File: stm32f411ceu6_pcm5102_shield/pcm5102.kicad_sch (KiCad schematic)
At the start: 29 parts, among them J200 AudioJack3_Ground_SwitchTR, J201 Conn_01x03_Pin, SW200 SW_DPDT_XLX, U200 PCM5102A, U201 HT7533-1

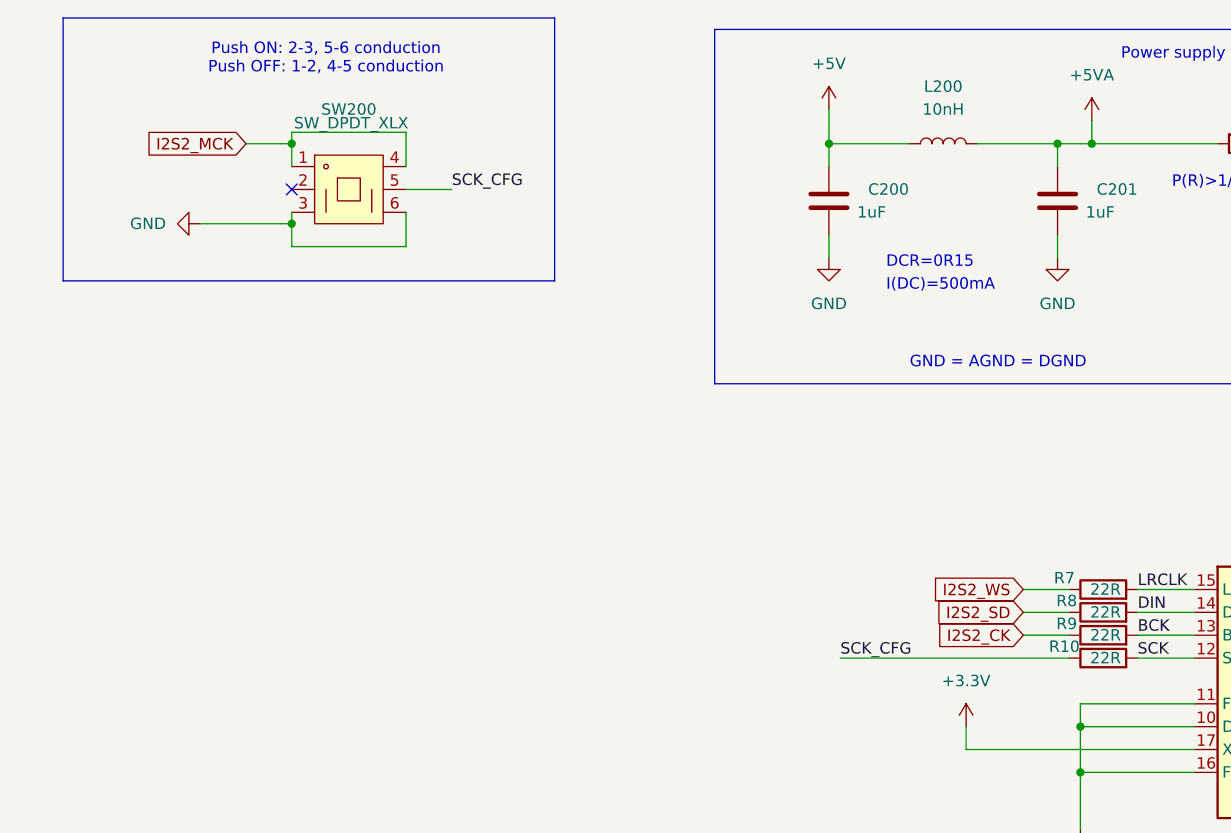
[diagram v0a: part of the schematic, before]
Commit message: First PCB routing
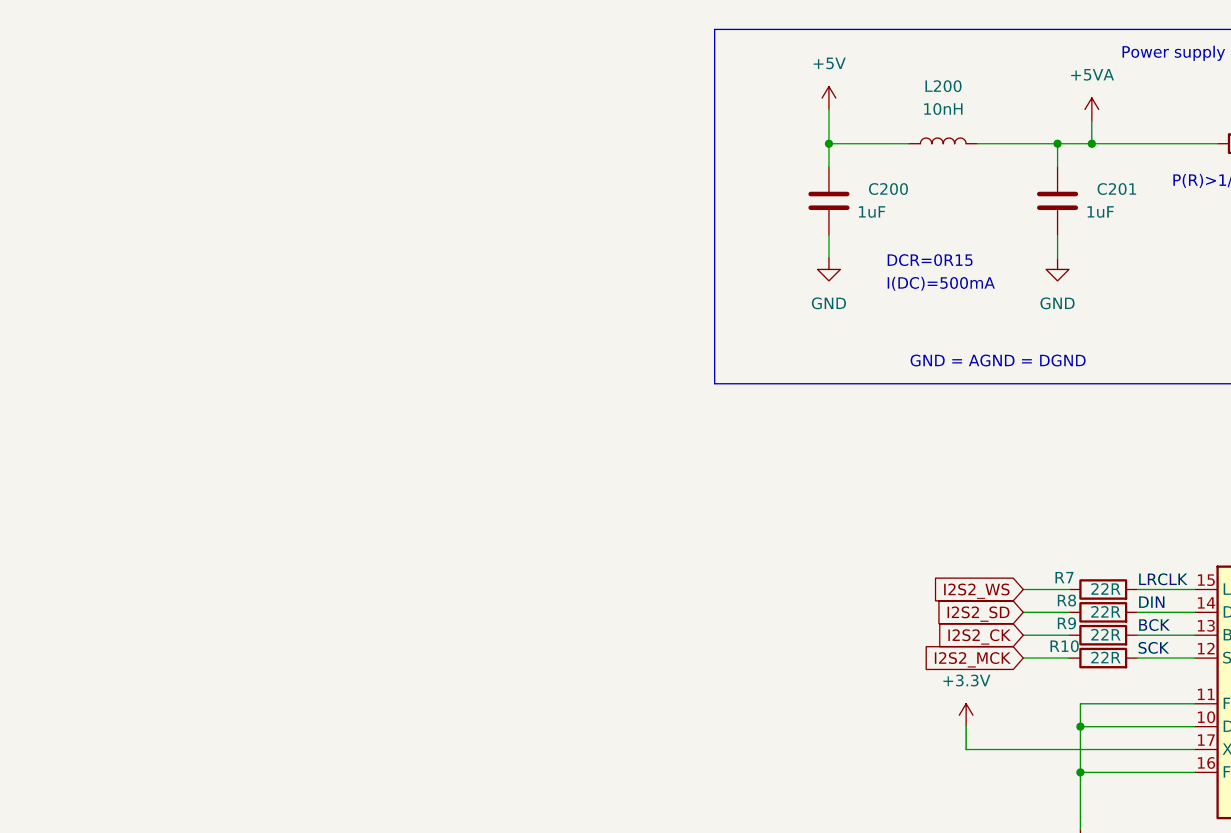
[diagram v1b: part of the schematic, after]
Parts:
- removed SW200: SW_DPDT_XLX, stm32f401_pcm5102_shiled_lib:SW_DPDT_XLX, symbol stm32f401_pcm5102_shiled_lib:SW_DPDT_XLX
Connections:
- net SCK_CFG is gone; now on net I2S2_MCK: R10.1
- no-connect marks 1 -> 0
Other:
- note removed: "Push ON: 2-3, 5-6 conduction Push OFF: 1-2, 4-5 conduction"

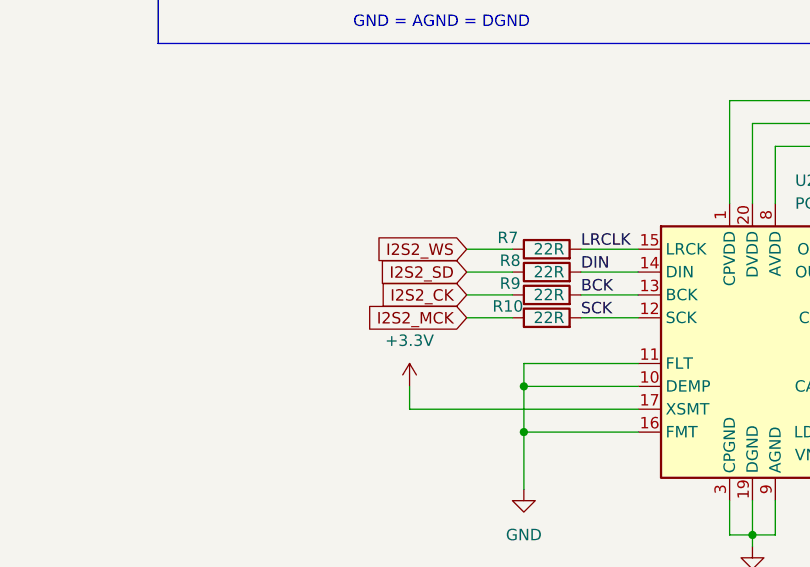
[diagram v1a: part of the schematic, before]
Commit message: Update firmware to simplify routing
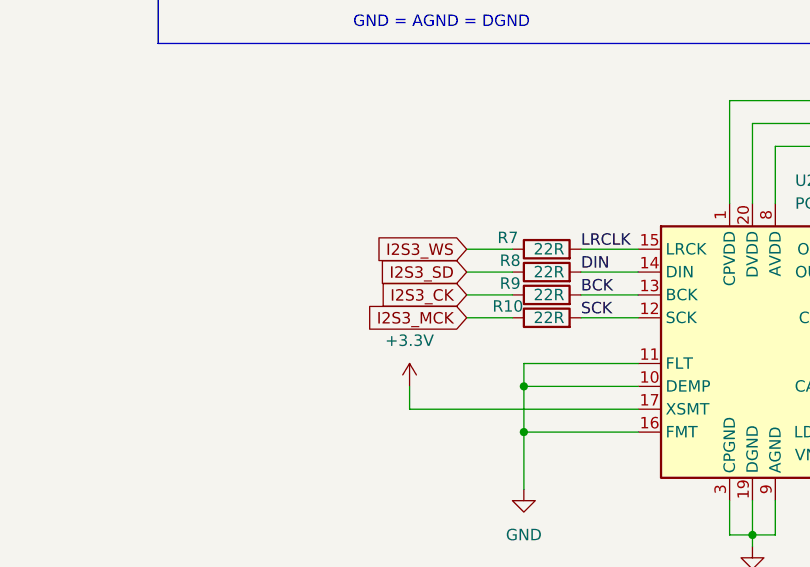
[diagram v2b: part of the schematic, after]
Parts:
- R10, R7, R8, R9: footprint Resistor_SMD:R_0805_2012Metric -> Resistor_SMD:R_0603_1608Metric
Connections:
- net I2S2_CK renamed I2S3_CK
- net I2S2_MCK renamed I2S3_MCK
- net I2S2_SD renamed I2S3_SD
- net I2S2_WS renamed I2S3_WS
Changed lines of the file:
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@@
 		)
 	)
-	(global_label "I2S2_CK"
+	(global_label "I2S3_CK"
 		(shape input)
 		(at 120.65 81.28 180)
@@
 		)
 	)
-	(global_label "I2S2_SD"
+	(global_label "I2S3_SD"
 		(shape input)
 		(at 120.65 78.74 180)
@@
 		)
 	)
-	(global_label "I2S2_WS"
+	(global_label "I2S3_WS"
 		(shape input)
 		(at 120.65 76.2 180)
@@
 		)
 	)
-	(global_label "I2S2_MCK"
+	(global_label "I2S3_MCK"
 		(shape input)
 		(at 120.65 83.82 180)
@@
 			)
 		)
-		(property "Footprint" "Resistor_SMD:R_0805_2012Metric"
+		(property "Footprint" "Resistor_SMD:R_0603_1608Metric"
 			(at 129.54 83.058 90)
 			(effects
@@
 			)
 		)
-		(property "Footprint" "Resistor_SMD:R_0805_2012Metric"
+		(property "Footprint" "Resistor_SMD:R_0603_1608Metric"
 			(at 129.54 85.598 90)
 			(effects
@@
 			)
 		)
-		(property "Footprint" "Resistor_SMD:R_0805_2012Metric"
+		(property "Footprint" "Resistor_SMD:R_0603_1608Metric"
 			(at 129.54 77.978 90)
 			(effects
@@
 			)
 		)
-		(property "Footprint" "Resistor_SMD:R_0805_2012Metric"
+		(property "Footprint" "Resistor_SMD:R_0603_1608Metric"
 			(at 129.54 80.518 90)
 			(effects

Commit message: BOM fixes
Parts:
- R10, R7, R8, R9: Manufacturer Part Number 0805W8F220JT5E -> 0603WAF220JT5E
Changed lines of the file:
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@@
 			)
 		)
-		(property "Manufacturer Part Number" "0805W8F220JT5E"
+		(property "Manufacturer Part Number" "0603WAF220JT5E"
 			(at 129.54 81.28 0)
 			(effects
@@
 			)
 		)
-		(property "Manufacturer Part Number" "0805W8F220JT5E"
+		(property "Manufacturer Part Number" "0603WAF220JT5E"
 			(at 129.54 83.82 0)
 			(effects
@@
 			)
 		)
-		(property "Manufacturer Part Number" "0805W8F220JT5E"
+		(property "Manufacturer Part Number" "0603WAF220JT5E"
 			(at 129.54 76.2 0)
 			(effects
@@
 			)
 		)
-		(property "Manufacturer Part Number" "0805W8F220JT5E"
+		(property "Manufacturer Part Number" "0603WAF220JT5E"
 			(at 129.54 78.74 0)
 			(effects
